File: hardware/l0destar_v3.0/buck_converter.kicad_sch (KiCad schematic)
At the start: 11 parts

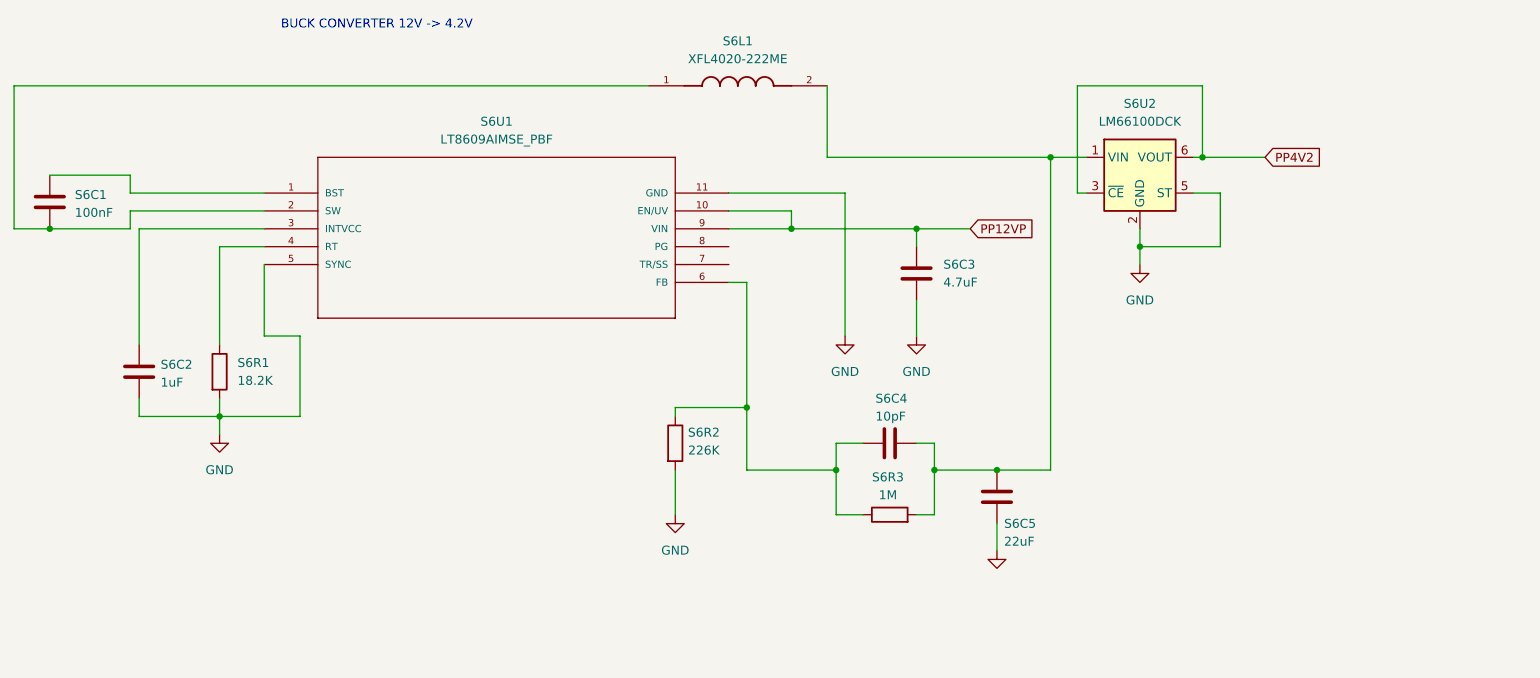
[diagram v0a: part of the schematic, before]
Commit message: updated v3.0 part specifications and added to the schematics
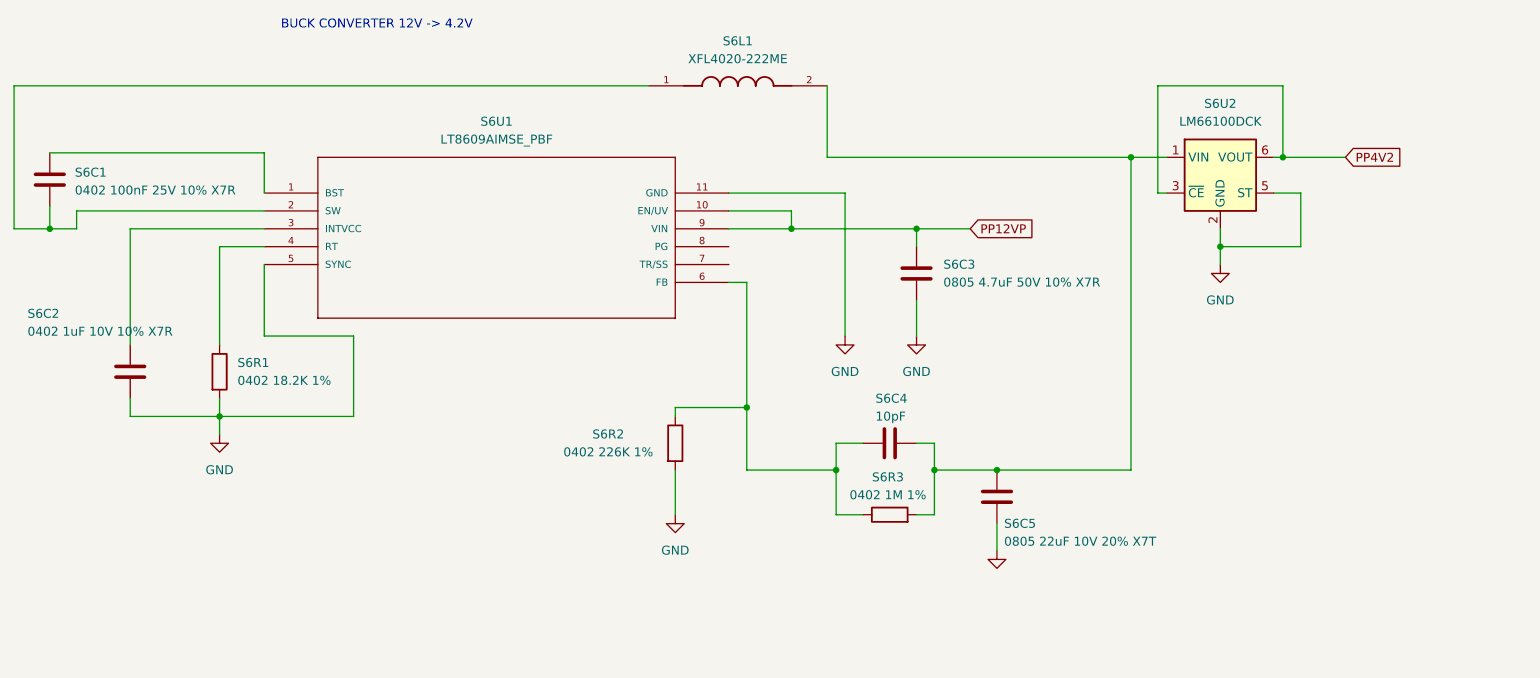
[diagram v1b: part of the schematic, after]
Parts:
- S6C1: value 100nF -> 0402 100nF 25V 10% X7R
- S6C2: value 1uF -> 0402 1uF 10V 10% X7R
- S6C3: value 4.7uF -> 0805 4.7uF 50V 10% X7R
- S6C5: value 22uF -> 0805 22uF 10V 20% X7T
- S6R1: value 18.2K -> 0402 18.2K 1%
- S6R2: value 226K -> 0402 226K 1%
- S6R3: value 1M -> 0402 1M 1%
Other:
- moved on the sheet: S6C1, S6C2, S6U2
